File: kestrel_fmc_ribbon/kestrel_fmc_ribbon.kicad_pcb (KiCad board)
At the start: 4 copper layers, 73.8 x 75 mm, 3 parts, among them J1 ASP-134602-01, J5 SHF-120-01-L-D-SM, J6 SHF-120-01-L-D-SM

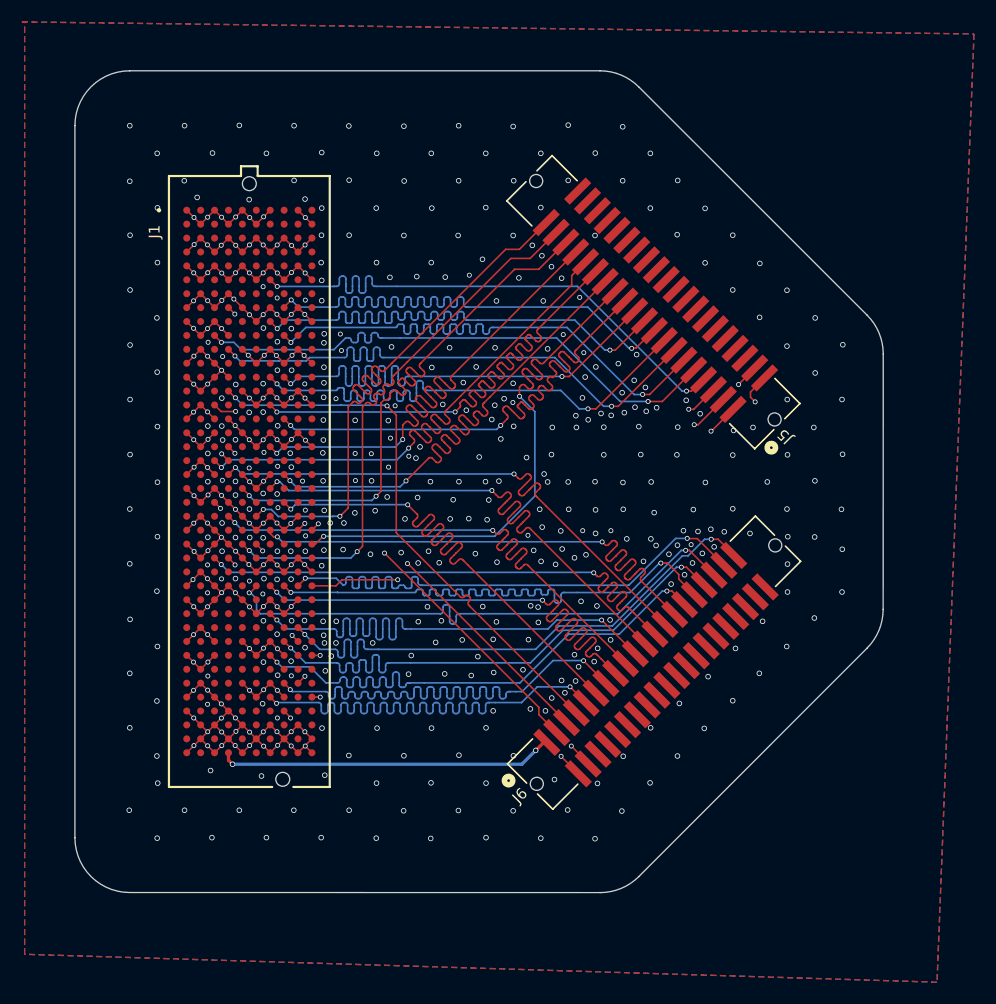
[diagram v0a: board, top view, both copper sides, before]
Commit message: removing outdated kicad project & maybe some design changes
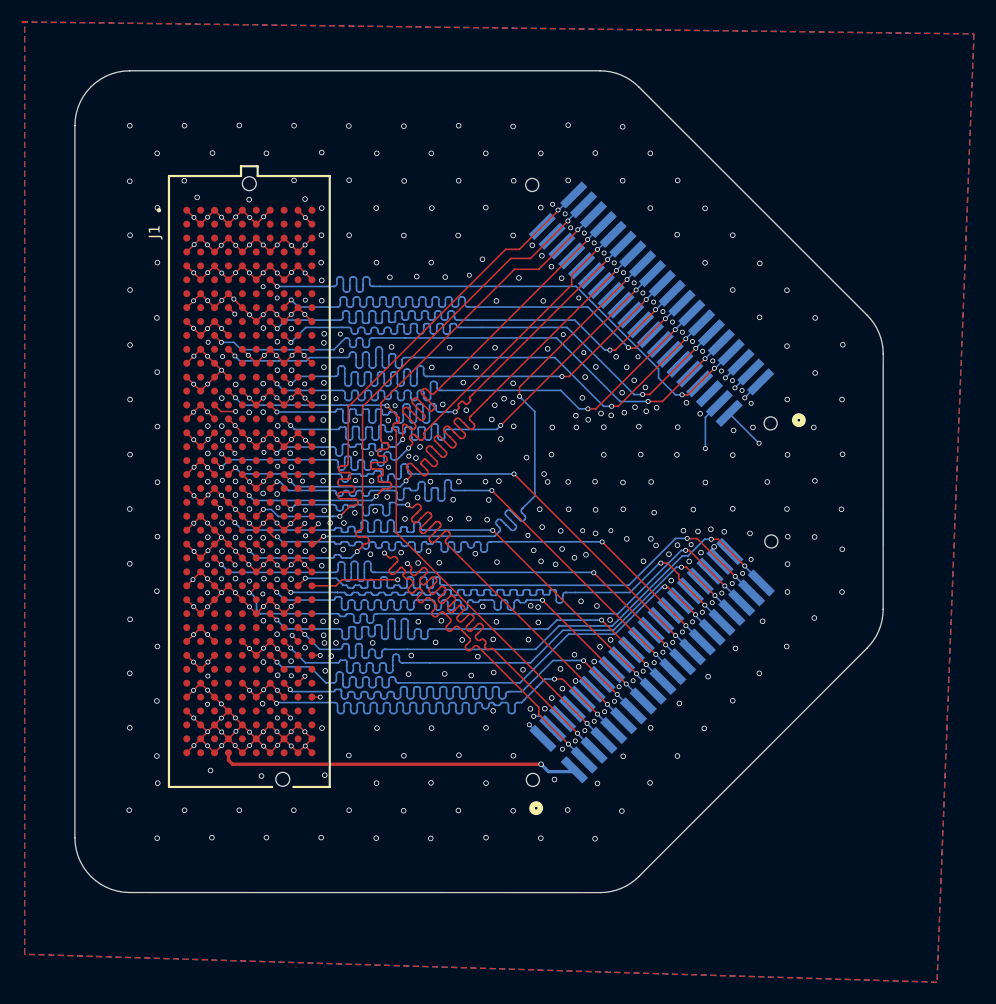
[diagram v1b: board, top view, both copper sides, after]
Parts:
- J5, J6: moved to B.Cu
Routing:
- net /SPI_MOSI: track 35.2 -> 54.6 mm, vias 2 -> 3
- net /SPI_CLK: track 41.2 -> 54.6 mm, vias 2 -> 3
- net /D1_2: track 50.9 -> 59.0 mm, vias 2 -> 3
- net /D2_1: track 50.8 -> 58.8 mm, vias 2 -> 3
- net /SPI_MISO: track 46.0 -> 41.4 mm
- net /GPIO3: track 50.3 -> 45.7 mm
- net /SPI_CS: track 63.4 -> 58.8 mm
- net /ENABLE: track 51.8 -> 55.3 mm
- net /GPIO4: track 71.6 -> 75.2 mm
- net /D4_6: track 50.8 -> 54.4 mm, vias 2 -> 3
- net /D2_4: track 50.8 -> 54.4 mm, vias 2 -> 3
- net /D1_5: track 50.7 -> 54.2 mm, vias 2 -> 3
- net /D3_4: track 50.9 -> 54.4 mm, vias 2 -> 3
- net /D3_2: track 50.5 -> 54.0 mm, vias 2 -> 3
- net /D2_6: track 50.9 -> 54.4 mm, vias 2 -> 3
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
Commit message: fmc gerber
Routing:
- net GND: vias 589 -> 585

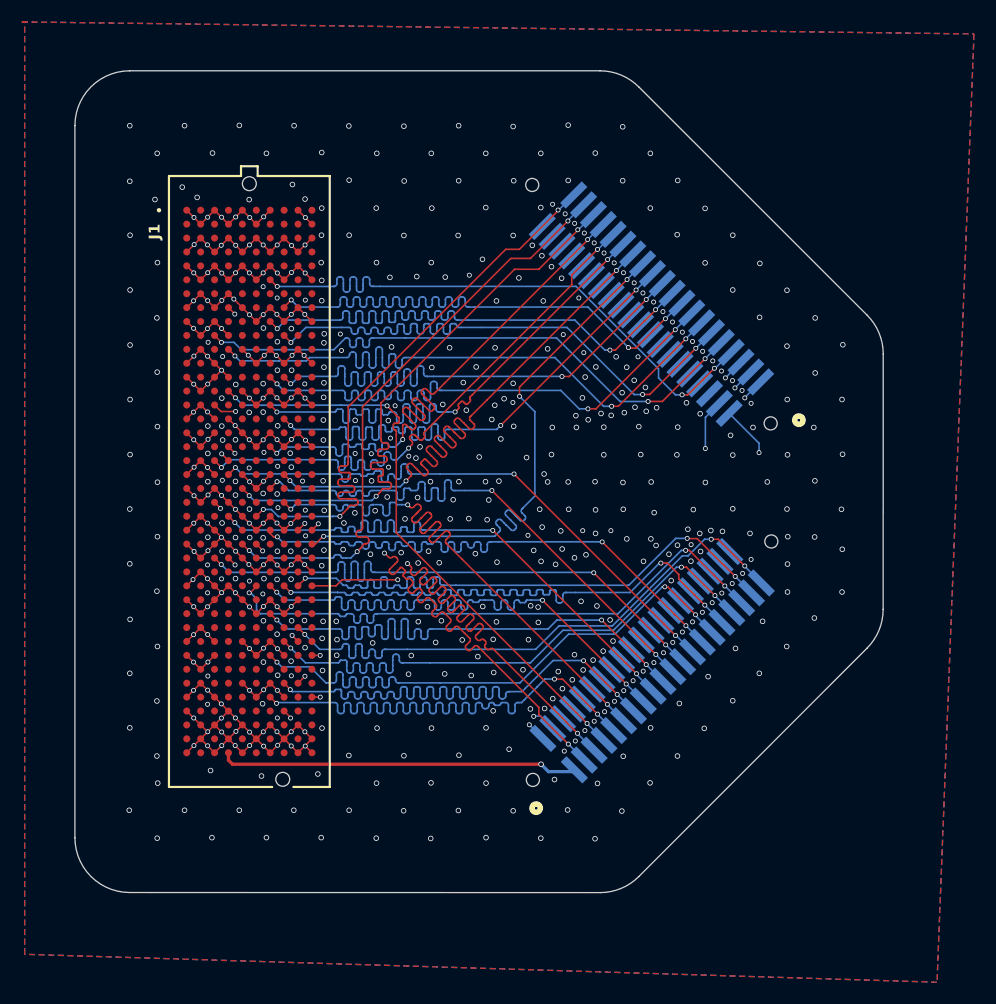
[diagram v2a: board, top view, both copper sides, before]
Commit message: fmc adapter redesign, add silkscreen to both pcbs
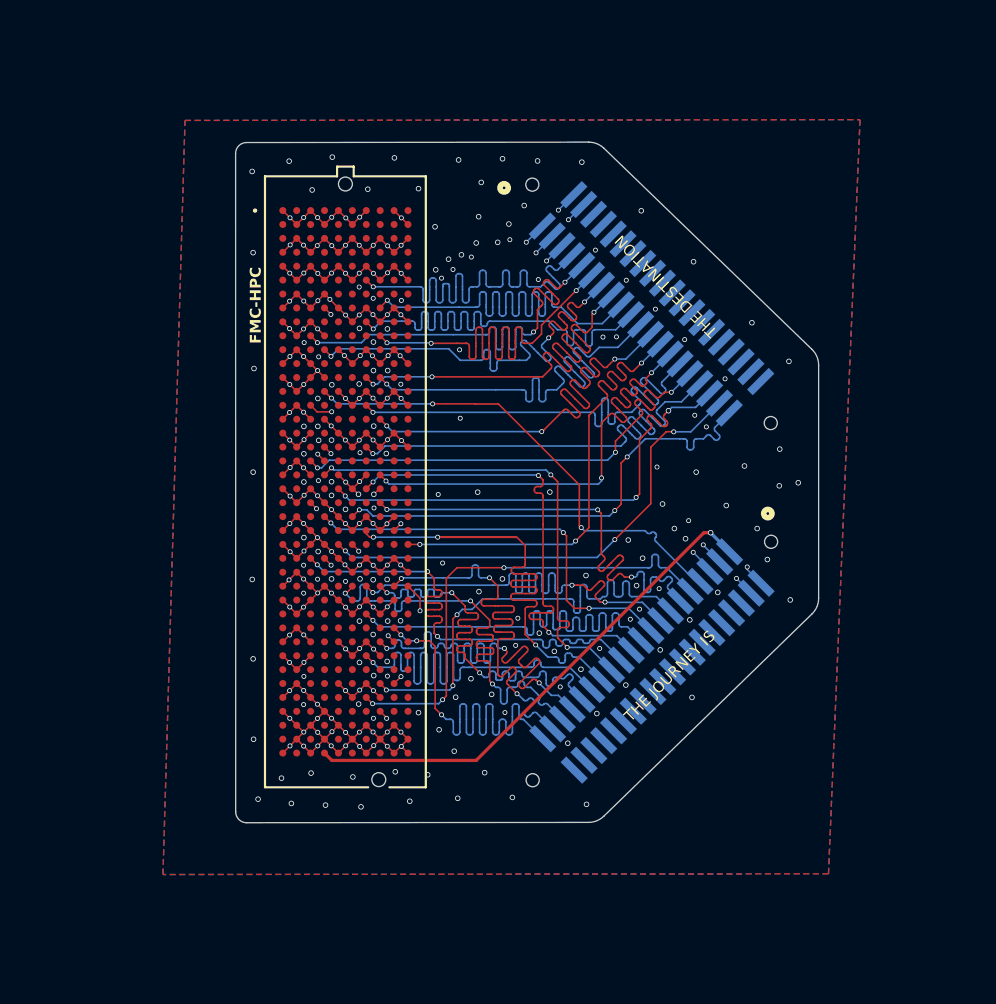
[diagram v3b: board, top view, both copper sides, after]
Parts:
- added G***: LOGO, LOGO, B.Cu at (131.6, 93.0)
- moved FMC-HPC 8.77 mm to (118.4, 88.9)
- moved J2 0.50 mm to (146.2, 105.1), turned to -135 degrees
- moved J1 0.48 mm to (146.1, 72.8), turned to -45 degrees
- renumbered J1 to FMC-HPC, J5 to J1, J6 to J2
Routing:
- net /GPIO2: track 79.6 -> 49.1 mm, vias 2 -> 4
- net /GPIO4: track 75.2 -> 45.7 mm, vias 2 -> 4
- net /SPI_MOSI: track 54.6 -> 34.2 mm, vias 3 -> 2
- net /ENABLE: track 55.3 -> 37.1 mm, vias 2 -> 4
- net /D3_4: track 54.4 -> 37.6 mm
- net /D1_2: track 59.0 -> 43.9 mm
- net /D2_1: track 58.8 -> 44.0 mm
- net /V3V3: track 32.8 -> 46.6 mm
- net /SPI_CLK: track 54.6 -> 42.1 mm
- net /D4_4: track 54.4 -> 43.8 mm
- net /D4_3: track 54.1 -> 43.6 mm
- net /D4_7: track 54.4 -> 43.9 mm
- net /D3_7: track 54.4 -> 43.9 mm
- net /D1_0: track 54.4 -> 43.9 mm
- net /D4_6: track 54.4 -> 43.9 mm
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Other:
- board size 73.8 x 75 mm -> 53.2 x 62.1 mm
- board text added: "3V3"
- board text added: "D2_7"
- board text added: "D4_7"
- board text added: "EN"
- board text added: "KESTREL FMC ADAPTER V2 NEWMAN & RAMOS WWU EECE 2026"
- board text added: "THE DESTINATION"
- board text added: "THE JOURNEY IS"
